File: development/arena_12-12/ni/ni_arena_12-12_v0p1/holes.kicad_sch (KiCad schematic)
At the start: 6 parts

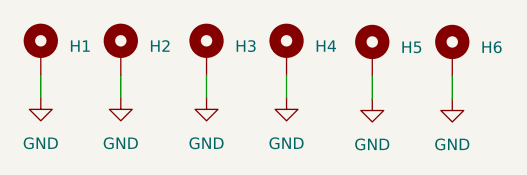
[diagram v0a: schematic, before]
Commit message: Worked on fabrication setup for NI 12-12 arena.
Added part numbers, datasheets, etc. to symbol table.
Deleted old productions files.
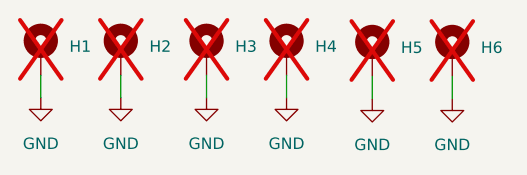
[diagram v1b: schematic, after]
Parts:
- H1, H2, H3, H4, H5, H6: now not fitted
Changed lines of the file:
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@@
 		(in_bom yes)
 		(on_board yes)
-		(dnp no)
+		(dnp yes)
 		(property "Reference" "H2"
 			(at 53.34 29.464 0)
@@
 		(in_bom yes)
 		(on_board yes)
-		(dnp no)
+		(dnp yes)
 		(fields_autoplaced yes)
 		(property "Reference" "H3"
@@
 		(in_bom yes)
 		(on_board yes)
-		(dnp no)
+		(dnp yes)
 		(fields_autoplaced yes)
 		(property "Reference" "H1"
@@
 		(in_bom yes)
 		(on_board yes)
-		(dnp no)
+		(dnp yes)
 		(fields_autoplaced yes)
 		(property "Reference" "H6"
@@
 		(in_bom yes)
 		(on_board yes)
-		(dnp no)
+		(dnp yes)
 		(fields_autoplaced yes)
 		(property "Reference" "H5"
@@
 		(in_bom yes)
 		(on_board yes)
-		(dnp no)
+		(dnp yes)
 		(fields_autoplaced yes)
 		(property "Reference" "H4"

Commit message: Finished preliminary production setup for NI 12-12 arena with schmitt buffers.
Note,  rotation offsets may still adjusting (for 74LVC2G17's and Q1)
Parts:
- H1, H2, H3, H4, H5, H6: now left out of the parts list
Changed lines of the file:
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@@
 		(unit 1)
 		(exclude_from_sim no)
-		(in_bom yes)
-		(on_board yes)
+		(in_bom no)
+		(on_board no)
 		(dnp yes)
 		(property "Reference" "H2"
@@
 		(unit 1)
 		(exclude_from_sim no)
-		(in_bom yes)
-		(on_board yes)
+		(in_bom no)
+		(on_board no)
 		(dnp yes)
 		(fields_autoplaced yes)
@@
 		(unit 1)
 		(exclude_from_sim no)
-		(in_bom yes)
-		(on_board yes)
+		(in_bom no)
+		(on_board no)
 		(dnp yes)
 		(fields_autoplaced yes)
@@
 		(unit 1)
 		(exclude_from_sim no)
-		(in_bom yes)
-		(on_board yes)
+		(in_bom no)
+		(on_board no)
 		(dnp yes)
 		(fields_autoplaced yes)
@@
 		(unit 1)
 		(exclude_from_sim no)
-		(in_bom yes)
-		(on_board yes)
+		(in_bom no)
+		(on_board no)
 		(dnp yes)
 		(fields_autoplaced yes)
@@
 		(unit 1)
 		(exclude_from_sim no)
-		(in_bom yes)
-		(on_board yes)
+		(in_bom no)
+		(on_board no)
 		(dnp yes)
 		(fields_autoplaced yes)

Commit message: project cleanup prior to ordering
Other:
- company: (none) -> IORodeo for Reiserlab @ Janelia
- title: (none) -> 12-12 NI G4.1 Arena Modular LED Display
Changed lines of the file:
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@@
 	(generator_version "9.0")
 	(paper "A4")
+	(title_block
+		(title "12-12 NI G4.1 Arena Modular LED Display")
+		(date "2025-04-21")
+		(rev "v0.3.4")
+		(company "IORodeo for Reiserlab @ Janelia")
+	)
 	(wire
 		(pts
